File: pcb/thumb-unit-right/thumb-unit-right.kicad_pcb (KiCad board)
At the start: 2 copper layers, 82.5 x 79 mm, 24 parts, among them J1 Conn_01x10, SW1 SW_SPDT, SW2 SW_Push, SW3 SW_Push, SW4 SW_Push, SW5 SW_Push, U1 xiao-ble, U2 PMW3610, U3 TLV70218_SOT23-5

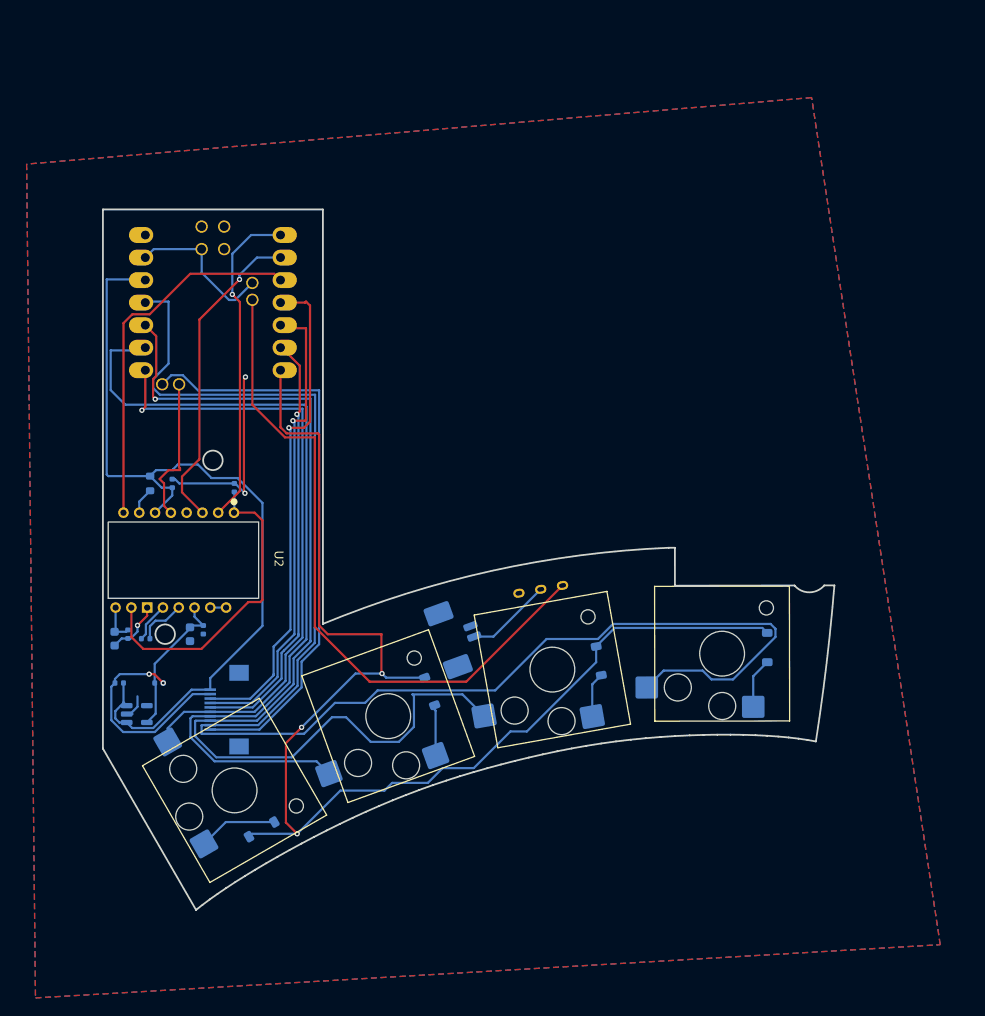
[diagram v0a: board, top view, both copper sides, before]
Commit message: fix(pcb/thumb-unit-right): GND pour, mirror PMW3610, swap to roBa XIAO footprint
- Schematic: switch U1 footprint from mcu:xiao-ble-tht to
  mcu_roba:XIAO_nRF52840_wBAT_wNFC_1 so back-side BAT_SW / NCS / COL4
  pads are exposed; tie XIAO 5V (pin 14) to no_connect since the
  battery path goes through SW1 → BAT_SW instead.
- PCB: align U2 (PMW3610) to (175.770, 103.150) so it mirrors the
  left half exactly (same XY, opposite layer), enabling a single
  trackball housing STL to be reused mirrored.
- PCB: add F.Cu GND zone covering the SMD side; clean up routing so
  every GND/+3V3/+1V8/SPI/matrix net resolves with zero unconnected
  pads.

DRC: 0 unconnected, 0 schematic-parity errors. Remaining warnings are
all environment-only (kicad-cli library path) or intentional
(copper_edge_clearance on U1 PTH pads 19-22 from the roBa
castellation cutout).

Co-Authored-By: Claude Opus 4.7 (1M context) <noreply@anthropic.com>
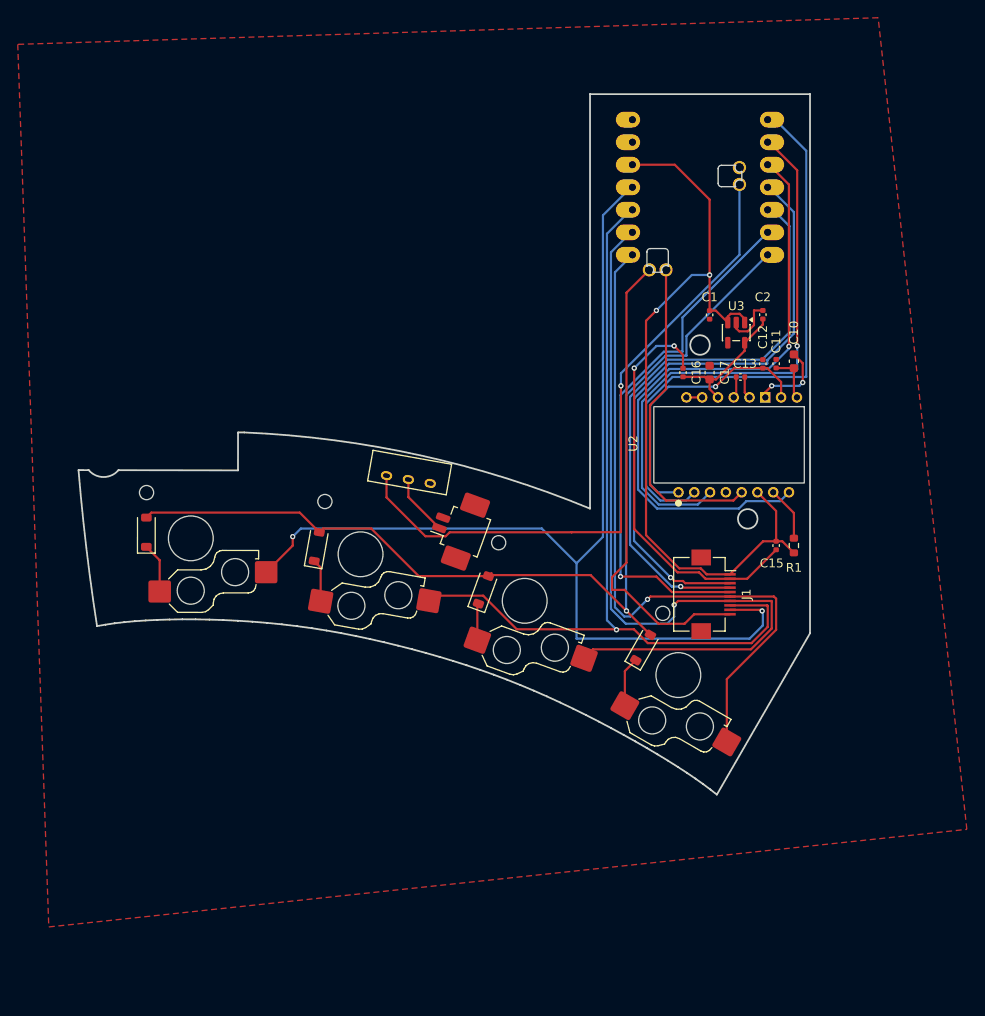
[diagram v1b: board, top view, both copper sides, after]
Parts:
- BT1, C1, C10, C11, C12, C13, C15, C16, C17, C2, D1, D2, D3, D4, J1, R1, SW1, U3: moved to F.Cu
- SW2, SW3, SW4, SW5: moved to B.Cu
- U1: footprint mcu:xiao-ble-tht -> mcu_roba:XIAO_nRF52840_wBAT_wNFC_1
- moved C10 82.7 mm to (184.5, 93.7), turned to -90 degrees
- moved U3 80.1 mm to (178.0, 90.5), turned to -90 degrees
- moved C2 79.7 mm to (181.0, 88.5), turned to -90 degrees
- moved C11 79.2 mm to (182.5, 94.0), turned to -90 degrees
- moved C1 78.4 mm to (175.0, 88.5), turned to 90 degrees
- moved C13 73.3 mm to (178.5, 95.5), turned to 0 degrees
- moved R1 72.9 mm to (184.5, 114.5), turned to 90 degrees
- moved D4 71.2 mm to (111.5, 113.0), turned to 89.9 degrees
- moved C15 68.4 mm to (182.5, 114.5), turned to 90 degrees
- moved C17 65.6 mm to (175.0, 95.0), turned to 90 degrees
- moved C16 61.4 mm to (172.0, 95.0), turned to 90 degrees
- moved SW5 61.3 mm to (116.5, 113.7), turned to -0.1 degrees
- moved C12 61.2 mm to (181.0, 94.0)
- moved U2 60.1 mm to (175.8, 103.2), turned to 90 degrees
- moved U1 59.7 mm to (173.9, 63.6)
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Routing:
- net /COL3: track 168.2 -> 119.8 mm, vias 0 -> 2
- net /ROW3: track 143.7 -> 111.9 mm, vias 3 -> 1
- net /SDIO: track 36.9 -> 67.4 mm, vias 1 -> 0
- net /SCLK: track 36.0 -> 64.8 mm
- net /MOTION: track 41.8 -> 70.0 mm, vias 0 -> 1
- net /COL2: track 116.8 -> 97.1 mm
- net /NCS: track 17.1 -> 36.4 mm
- net GND: track 73.8 -> 60.9 mm, vias 5 -> 4
- net /COL4: track 65.7 -> 53.1 mm
- net /ROW1: track 53.7 -> 66.0 mm
- net /ROW0: track 56.7 -> 68.0 mm
- net /ROW2: track 49.4 -> 60.0 mm
- net /COL0: track 71.4 -> 78.6 mm
- net /COL1: track 95.5 -> 89.8 mm, vias 0 -> 1
- net +3V3: track 94.6 -> 89.3 mm, vias 0 -> 2
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- removed copper zone on B.Cu, net GND
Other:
- outline, holes or cut-outs redrawn
